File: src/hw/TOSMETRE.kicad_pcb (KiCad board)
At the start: 2 copper layers, 4.5 x 3.5 mm, 61 parts, among them J1 Barrel_Jack_Switch, J2 Conn_01x02_Male, J3 Conn_01x08_Male, J4 Conn_Coaxial, J5 Conn_01x05_Male, J6 Conn_01x02_Male, J7 Conn_Coaxial, SW1 SW_DIP_x01, U1 TPS70950DBVT, U2 18F1320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

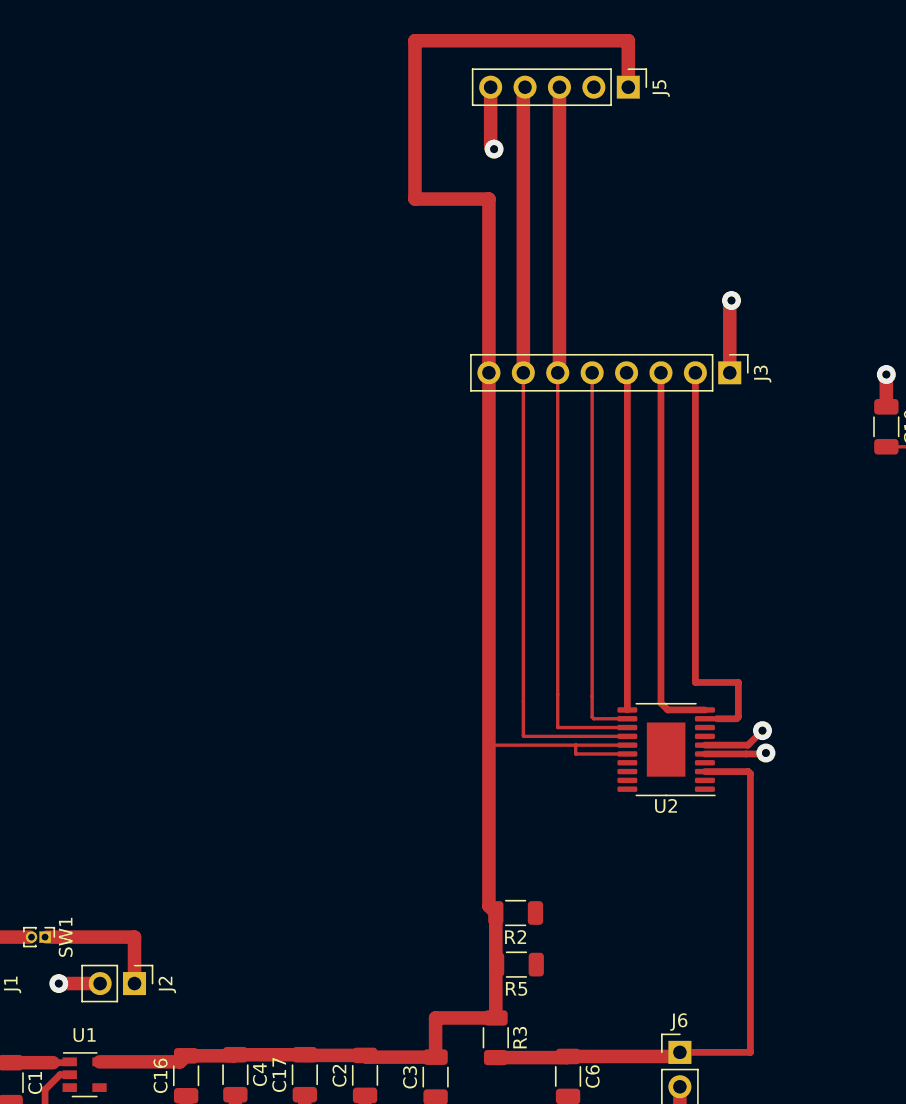
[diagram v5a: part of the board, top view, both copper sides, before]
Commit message: #304
MODIFICATION PCB AVEC NOUVELLE EMPREINTE J2 J3 ET J5
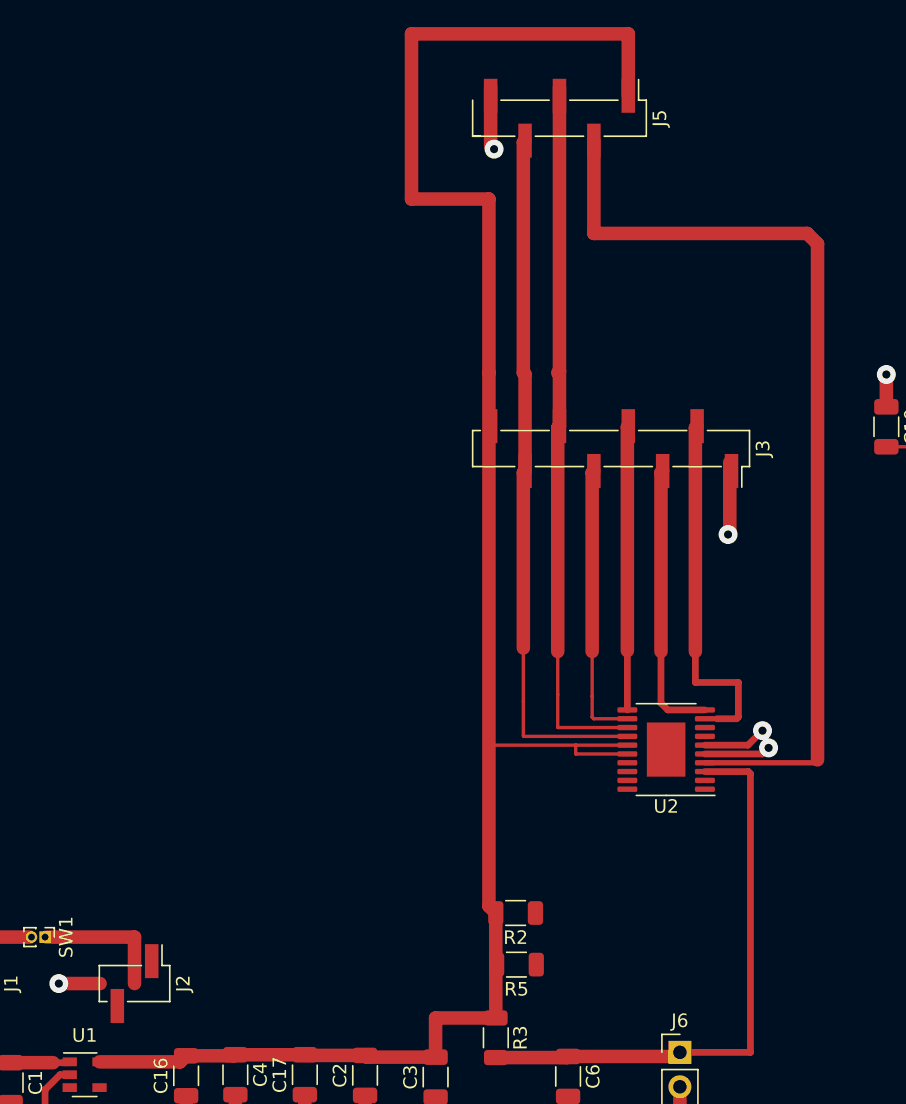
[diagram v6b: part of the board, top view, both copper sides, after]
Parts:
- J2: footprint Connector_PinHeader_2.54mm:PinHeader_1x02_P2.54mm_Vertical -> Connector_PinHeader_2.54mm:PinHeader_1x02_P2.54mm_Vertical_SMD_Pin1Left
- J3: footprint Connector_PinHeader_2.54mm:PinHeader_1x08_P2.54mm_Vertical -> Connector_PinHeader_2.54mm:PinHeader_1x08_P2.54mm_Vertical_SMD_Pin1Right
- J5: footprint Connector_PinHeader_2.54mm:PinHeader_1x05_P2.54mm_Vertical -> Connector_PinHeader_2.54mm:PinHeader_1x05_P2.54mm_Vertical_SMD_Pin1Left
- moved J3 10.4 mm to (140.7, 49.2)
- moved J5 5.57 mm to (136.9, 24.8)
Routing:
- net Net-(J5-Pad2): track 0.00 -> 70.2 mm
- net Net-(J3-Pad6): track 52.4 -> 73.2 mm
- net Net-(J3-Pad7): track 55.6 -> 72.1 mm
- net Net-(J3-Pad5): track 28.1 -> 20.9 mm
- net Net-(J3-Pad3): track 27.8 -> 20.6 mm
- net Net-(J3-Pad4): track 24.9 -> 21.0 mm
- net Net-(J3-Pad2): track 30.2 -> 26.4 mm
- net Net-(C10-Pad2): track 243.8 -> 246.0 mm

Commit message: #304
OUPS DES PETIT OUBLI
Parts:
- J1: footprint Connector_PinHeader_2.54mm:PinHeader_1x03_P2.54mm_Vertical -> Connector_PinHeader_2.54mm:PinHeader_1x03_P2.54mm_Vertical_SMD_Pin1Left
- J6: footprint Connector_PinHeader_2.54mm:PinHeader_1x02_P2.54mm_Vertical -> Connector_PinHeader_2.54mm:PinHeader_1x02_P2.54mm_Vertical_SMD_Pin1Left
- moved J1 13.3 mm to (83.8, 97.0), turned to 180 degrees
- moved J2 2.36 mm to (106.4, 86.5), turned to 0 degrees
- moved J6 1.65 mm to (146.4, 95.2)
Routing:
- net Net-(J1-Pad3): track 12.1 -> 21.3 mm
- net GNDREF: track 146.3 -> 150.4 mm
- net Net-(D1-Pad2): track 13.3 -> 9.64 mm
- net Net-(J2-Pad1): track 9.91 -> 6.48 mm

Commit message: #305
Livraison suite a coup de telephone
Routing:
- net Net-(R16-Pad1): track 20.5 -> 30.7 mm
- net GNDREF: track 150.4 -> 151.5 mm, vias 47 -> 46
